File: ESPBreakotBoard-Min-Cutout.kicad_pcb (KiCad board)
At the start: 2 copper layers, 26.9 x 29.9 mm, 14 parts, among them J1 Screw_Terminal_01x02, J2 Conn_01x08_Male, J3 Conn_01x08_Male, M2 MountingHole_2.2mm_M2_Pad_Via, U1 AMS1117-3.3, U2 ESP-07

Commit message: v3r4: Made some font improvements after 1st print and realizing a few labels were too small
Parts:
- added G***: LOGO, Andys-Footprints:Yoshi-Egg-Small, F.Cu at (161.4, 90.3)
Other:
- board text added: "Place 0Ω o. bridge"
- board text added: "Timed deep sleep:"
- board text added: "v3r4"
- board text removed: "JLCJLCJLCJLC"
- board text removed: "Timed deep sleep: Place 0Ω o. bridge"
- board text removed: "v3r3"

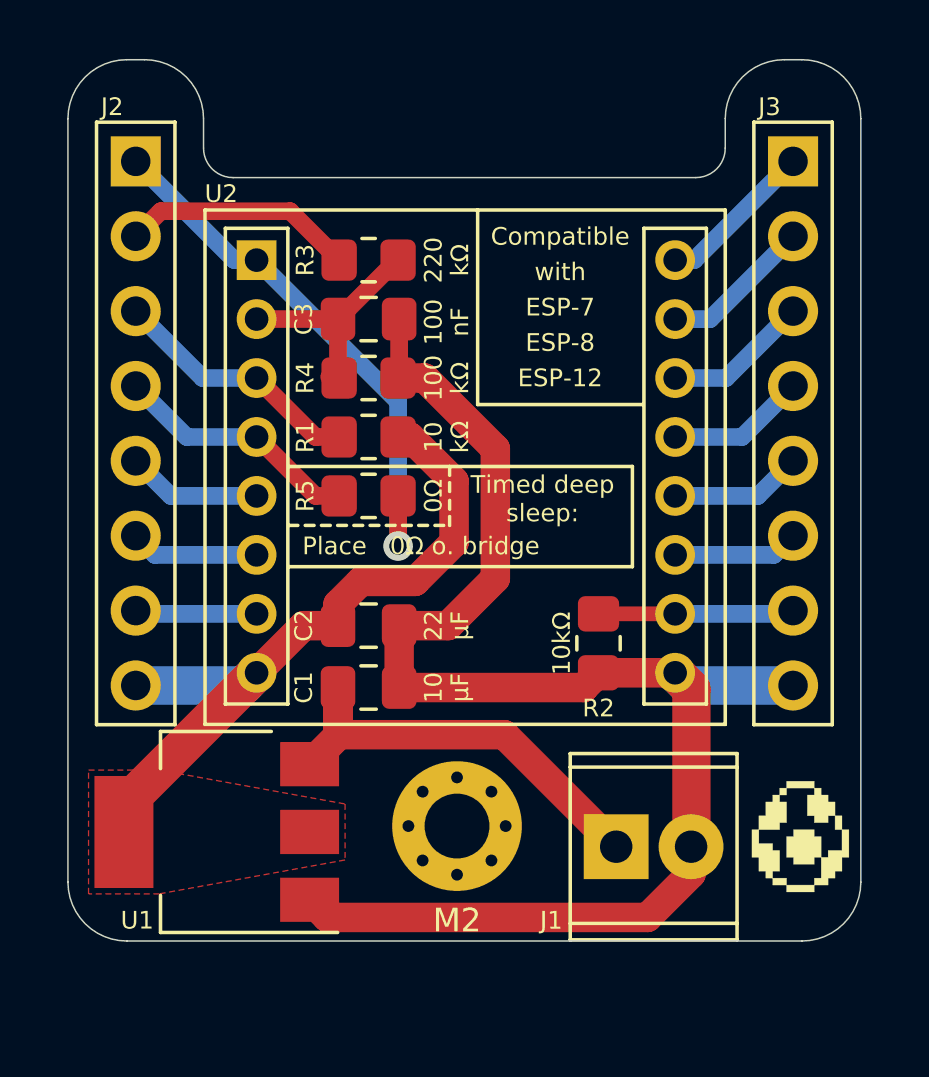
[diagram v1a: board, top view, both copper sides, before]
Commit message: v4r1: Added IO 9&10, made board a factor of 2.54mm; KiCad 6 update
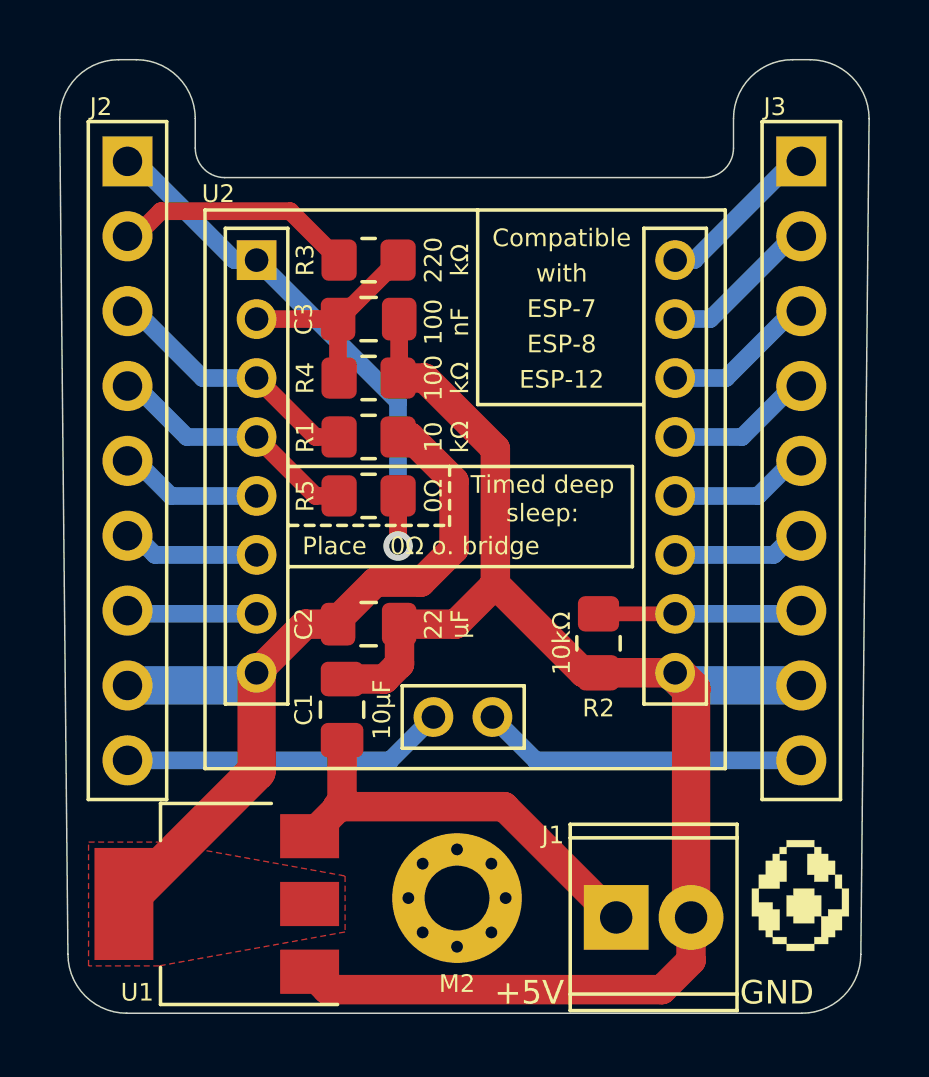
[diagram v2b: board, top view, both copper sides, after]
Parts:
- C1: value 10 -> 10µF
- J2, J3: value Conn_01x08_Male -> Conn_01x09_Male; footprint Andys-Footprints:PinHeader_1x08_P2.54mm_Vertical-Fixed-SilkScreen-Fixed-SilkScreen -> Andys-Footprints:PinHeader_1x09_P2.54mm_Vertical-Fixed-SilkScreen
- U2: footprint Andys-Footprints:ESP-07-Socket-Cutout -> Andys-Footprints:ESP-12-Socket-Cutout-IO9-10
- moved M2 2.44 mm to (149.8, 92.4)
- moved U1 2.44 mm to (141.7, 92.6)
- moved J1 2.40 mm to (155.2, 93.1)
- moved G*** 2.00 mm to (161.4, 92.3)
- moved C1 1.17 mm to (145.9, 86.0), turned to 90 degrees
- moved J2 0.28 mm to (138.6, 67.5)
- moved J3 0.28 mm to (161.5, 67.5)
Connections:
- J3 pad 1: Net-(J3-Pad1) -> Net-(U2-Pad22)
- J3 pad 2: Net-(J3-Pad2) -> Net-(U2-Pad21)
- J3 pad 3: Net-(J3-Pad3) -> Net-(U2-Pad20)
- J3 pad 4: Net-(J3-Pad4) -> Net-(U2-Pad19)
- J3 pad 5: Net-(J3-Pad5) -> Net-(U2-Pad18)
- J3 pad 6: Net-(J3-Pad6) -> Net-(U2-Pad17)
- U2 pad 11: Net-(J3-Pad6) -> Net-(U2-Pad11)
- U2 pad 12: Net-(J3-Pad5) -> Net-(U2-Pad12)
- U2 pad 15: Net-(J3-Pad2) -> GND
- U2 pad 16: Net-(J3-Pad1) -> /IO15
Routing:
- net Net-(U2-Pad12): track 0.00 -> 11.1 mm
- net Net-(U2-Pad11): track 0.00 -> 11.0 mm
- net Net-(U2-Pad22): track 0.00 -> 5.84 mm
- net Net-(J3-Pad1): track 5.56 -> 0.00 mm
- net Net-(U2-Pad21): track 0.00 -> 5.44 mm
- net Net-(U2-Pad20): track 0.00 -> 5.22 mm
- net Net-(J3-Pad2): track 5.16 -> 0.00 mm
- net Net-(J3-Pad3): track 5.14 -> 0.00 mm
- net Net-(U2-Pad19): track 0.00 -> 5.00 mm
- net Net-(J3-Pad5): track 4.79 -> 0.00 mm
- net Net-(U2-Pad18): track 0.00 -> 4.77 mm
- net Net-(J3-Pad4): track 4.72 -> 0.00 mm
- net Net-(U2-Pad17): track 0.00 -> 4.55 mm
- net Net-(J3-Pad6): track 4.27 -> 0.00 mm
- net GND: track 51.5 -> 53.8 mm
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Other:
- board size 26.9 x 29.9 mm -> 27.5 x 32.3 mm
- net class Default removed
- board text added: "+5V"
- board text added: "ADC"
- board text added: "Compatible"
- board text added: "EN"
- board text added: "ESP-12"
- board text added: "ESP-7"
- board text added: "ESP-8"
- board text added: "ESP8266 Breakout Board 5V & ADC ready"
- board text added: "GND"
- board text added: "IO0"
- board text added: "IO1"
- board text added: "IO10"
- board text added: "IO12"
- board text added: "IO13"
- board text added: "IO14"
- board text added: "IO15"
- board text added: "IO16"
- board text added: "IO2"
- board text added: "IO3"
- board text added: "IO4"
- board text added: "IO5"
- board text added: "IO9"
- board text added: "JLCJLCJLCJLC"
- board text added: "RST"
- board text added: "VCC"
- board text added: "by Andy"
- board text added: "v4r1"
- board text added: "with"
- board text removed: "ESP8266 Breakout Board 5V & ADC ready by Andy"
- board text removed: "v3r4"

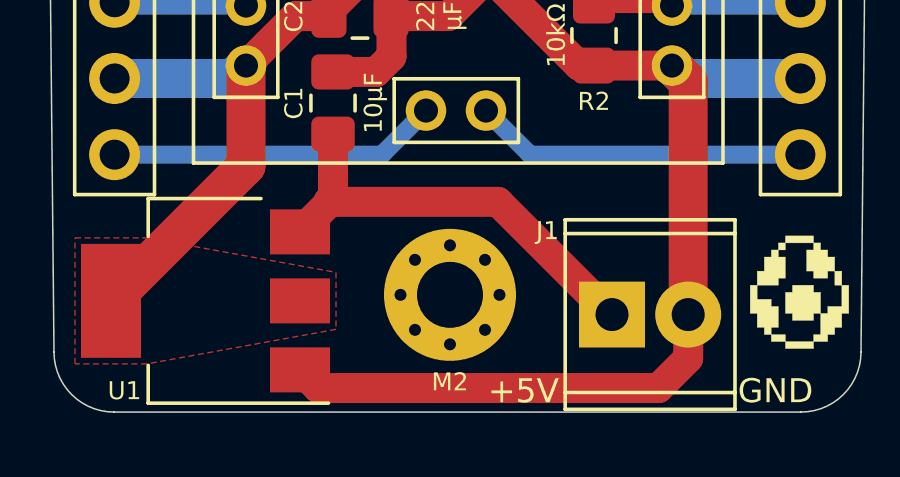
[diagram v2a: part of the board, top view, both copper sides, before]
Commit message: v4r2: Fixed Silkscreen and 3D Models
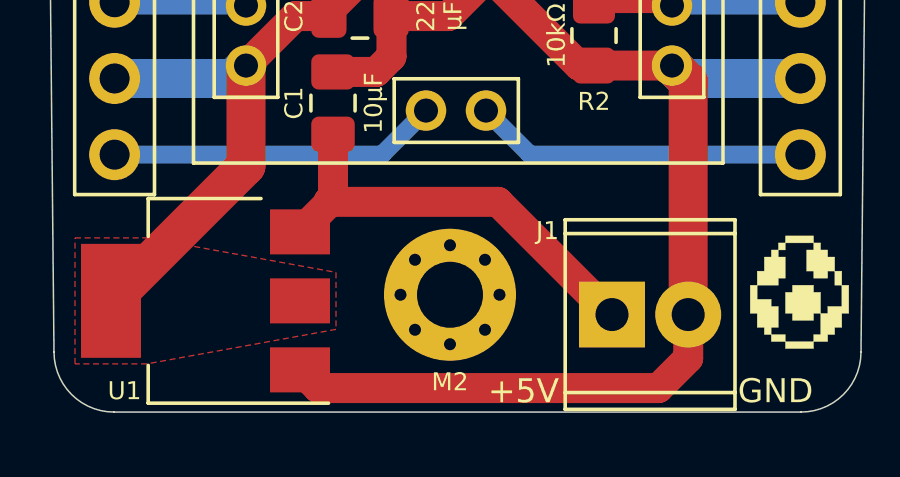
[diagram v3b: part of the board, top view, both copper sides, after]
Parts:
- removed M2: MountingHole_2.2mm_M2_Pad_Via, MountingHole:MountingHole_2.2mm_M2_Pad_Via
- added H1: M2, MountingHole:MountingHole_2.2mm_M2_Pad_Via, F.Cu at (149.8, 92.4)
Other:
- board text added: "v4r2"
- board text removed: "v4r1"
